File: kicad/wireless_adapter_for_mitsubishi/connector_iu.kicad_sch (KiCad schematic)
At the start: 7 parts, among them J1 S05B-PASK-2(LF)(SN), U3 TVS1400DRVR, U4 TVS0500DRVR

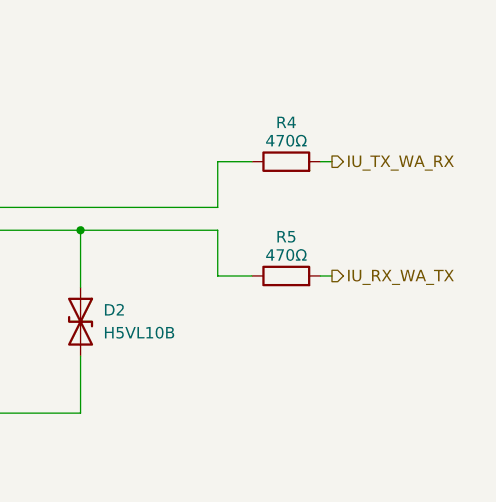
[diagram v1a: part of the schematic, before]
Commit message: Rename some KiCad buses.
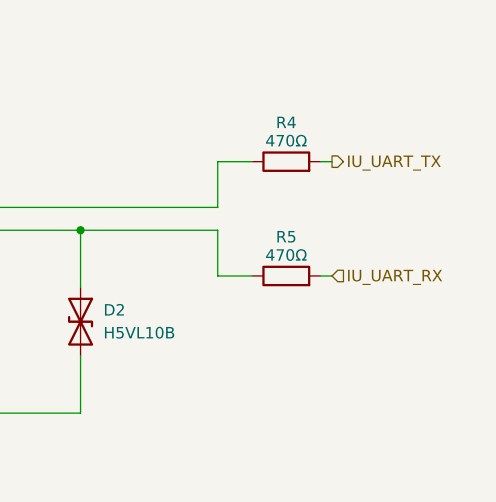
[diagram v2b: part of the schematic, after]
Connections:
- net IU_RX_WA_TX renamed IU_UART_RX
- net IU_TX_WA_RX renamed IU_UART_TX
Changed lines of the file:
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@@
 		)
 	)
-	(hierarchical_label "IU_RX_WA_TX"
-		(shape output)
+	(hierarchical_label "IU_UART_RX"
+		(shape input)
 		(at 205.74 99.06 0)
 		(effects
@@
 		)
 	)
-	(hierarchical_label "IU_TX_WA_RX"
+	(hierarchical_label "IU_UART_TX"
 		(shape output)
 		(at 205.74 86.36 0)
